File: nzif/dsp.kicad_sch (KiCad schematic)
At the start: 31 parts, among them U2 ADAU1467WBCPZ300

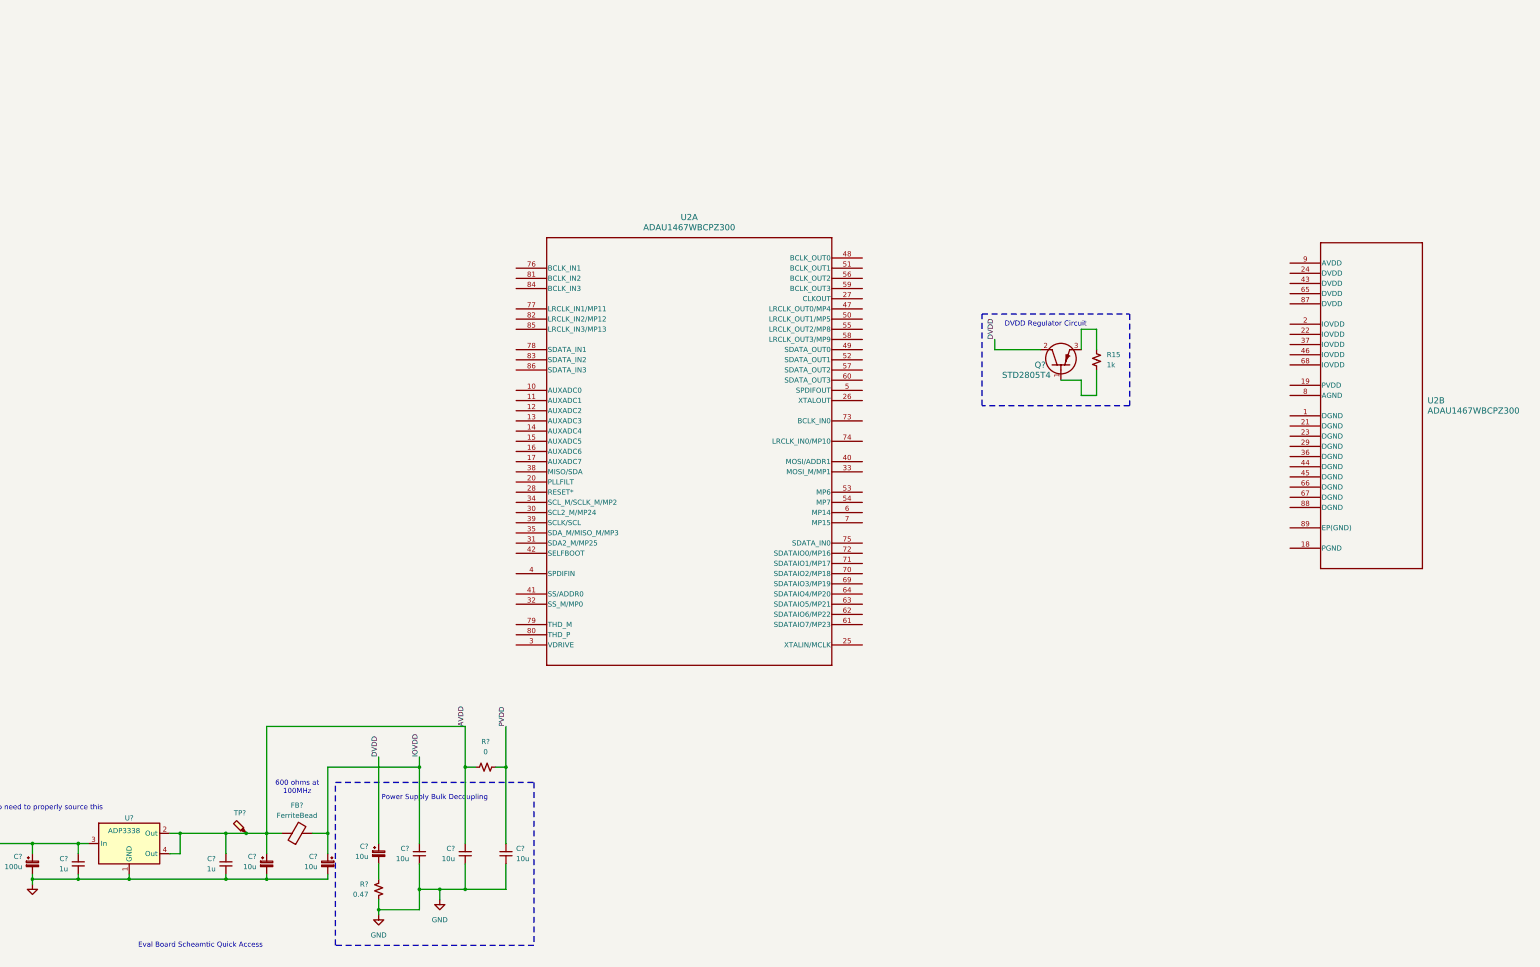
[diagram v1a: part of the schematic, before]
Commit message: Made adau1467 symbol klc compliant (ref #3)
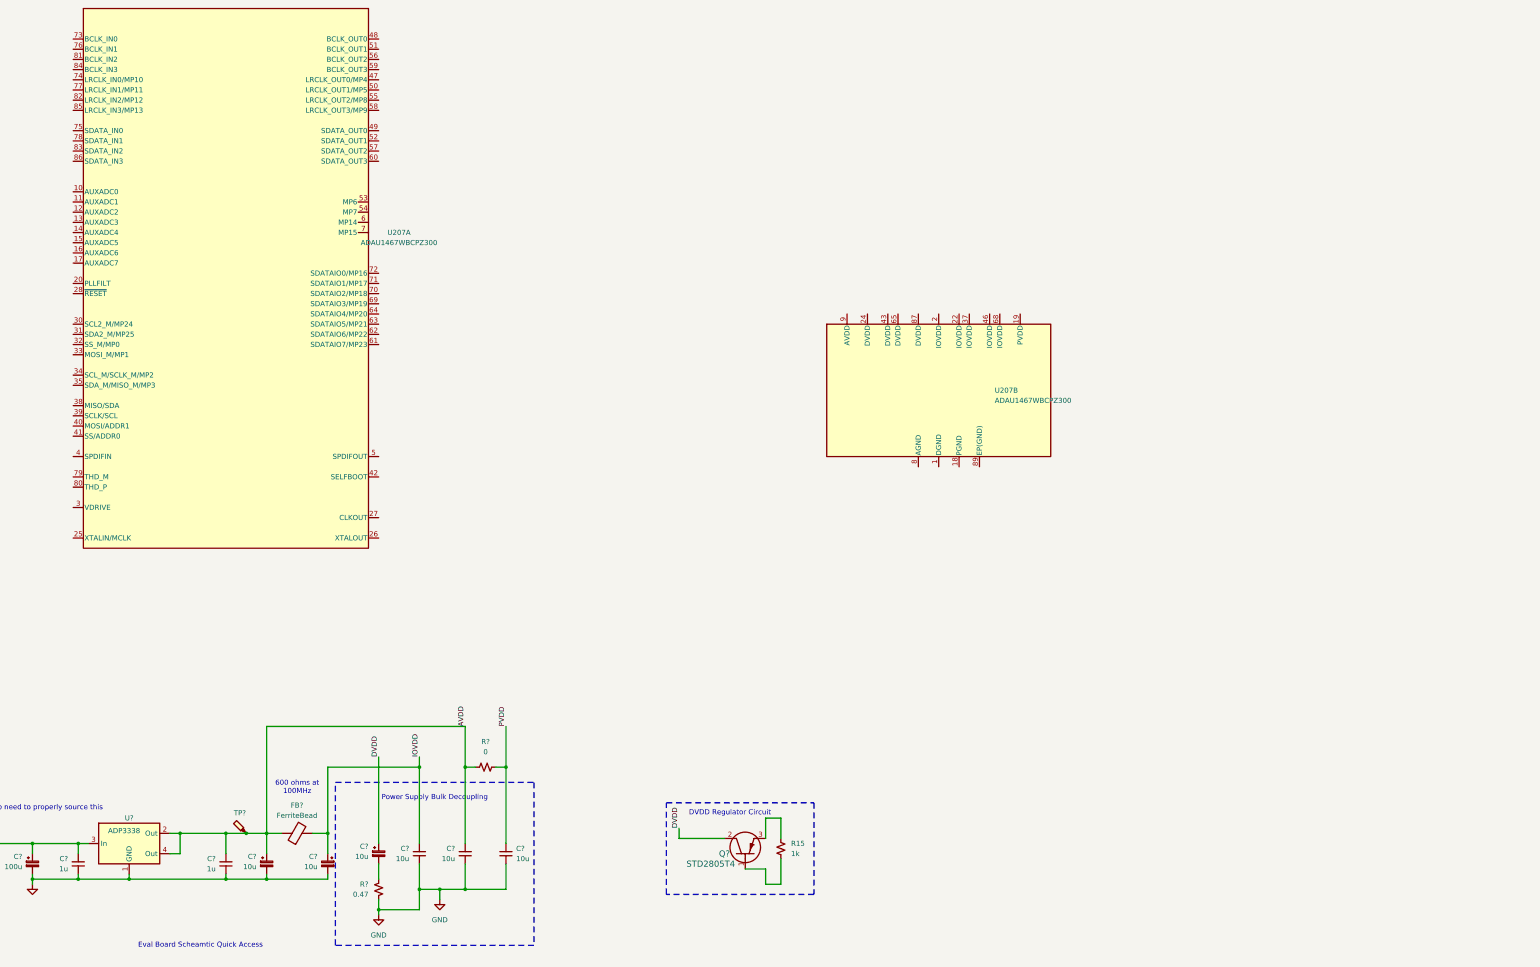
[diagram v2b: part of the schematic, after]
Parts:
- removed U2: ADAU1467WBCPZ300, CP_88_10_ADI, symbol ADAU1467:ADAU1467WBCPZ300
- added U207: ADAU1467WBCPZ300, CP_88_10_ADI, symbol nzif_radio_symbol_library:ADAU1467WBCPZ300
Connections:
- new net DGND: U207.1 (DGND), U207.21 (DGND), U207.23 (DGND), U207.29 (DGND), U207.36 (DGND), U207.44 (DGND), U207.45 (DGND), U207.66 (DGND), U207.67 (DGND), U207.88 (DGND)
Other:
- moved on the sheet: Q?, R15

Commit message: dsp tdm channels 0-2 added
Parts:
- removed R15: 1k, symbol Device:R_Small_US
- removed R?: 0, symbol Device:R_Small_US
- added C209, C211, C213, C215, C217, C219, C221, C223, C225, C227, C229: .1u, symbol Device:C_Small_US
- added C210, C212, C214, C216, C218, C220, C222, C224, C226, C228, C230: 10n, symbol Device:C_Small_US
- added J201: Conn_01x10, Connector_PinHeader_2.54mm:PinHeader_2x05_P2.54mm_Vertical, symbol Connector_Generic:Conn_01x10
- added R209: 1k, symbol Device:R_Small_US
- added R210, R211, R212, R213, R214, R215, R216, R217: 33, symbol Device:R_Small_US
- added TP201: VDrive, symbol Connector:TestPoint
- added TP202: IOVDD, symbol Connector:TestPoint
- added TP203: DVDD, symbol Connector:TestPoint
- Q?: footprint hf-transceiver:DPAKTO-252_TYPEA_STM -> nzif_footprints:DPAKTO-252_TYPEA_STM; symbol hf-transceiver:STD2805T4 -> nzif_radio_symbol_library:STD2805T4
- R?: value 0.47 -> 47
- U207: footprint CP_88_10_ADI -> nzif_footprints:CP_88_10_ADI
- U?: footprint hf-transceiver:RA_4_ADI -> nzif_footprints:RA_4_ADI; symbol hf-transceiver:ADM811TARTZ-REEL7 -> nzif-a:ADM811TARTZ-REEL7
- U?: symbol hf-transceiver:ADP3338 -> nzif_radio_symbol_library:ADP3338
- U?: footprint DFN-S8_6x5MC_MCH -> nzif_footprints:DPAKTO-252_TYPEA_STM; symbol hf-transceiver:25AA1024-I_MF -> nzif_radio_symbol_library:25AA1024-I_MF
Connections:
- net GND is gone; now on net DGND: C?.1, C?.1, C?.1, C?.1, C?.1, C?.1, C?.2, C?.2, C?.2, C?.2, D?.1 (K), J?.10 (Pin_10), R?.2, R?.2, SW?.2, U?.1 (GND), U?.1 (GND), U?.4 (VSS)
- net PVDD is gone; now on net 3.3V_DSP: C?.2
- net DGND: now also U207.18 (PGND), U207.8 (AGND), U207.89 (EP(GND)), C209.2, C210.2, C211.2, C212.2, C213.2, C214.2, C215.2, C216.2, C217.2, C218.2, C219.2, C220.2, C221.2, C222.2, C223.2, C224.2, C225.2, C226.2, C227.2, C228.2, C229.2, C230.2, J201.1 (Pin_1), J201.2 (Pin_2), J201.4 (Pin_4), J201.6 (Pin_6)
- net DVDD: now also U207.24 (DVDD), U207.43 (DVDD), U207.65 (DVDD), U207.87 (DVDD), C211.1, C212.1, C213.1, C214.1, C215.1, C216.1, C217.1, C218.1, TP203.1
- net IOVDD: now also Q?.3 (Emitter), U207.2 (IOVDD), U207.22 (IOVDD), U207.37 (IOVDD), U207.46 (IOVDD), U207.68 (IOVDD), C221.1, C222.1, C223.1, C224.1, C225.1, C226.1, C227.1, C228.1, C229.1, C230.1, R209.2, TP202.1; no longer C?.1, FB?.2
- net 3.3V_DSP: now reaches U207.19 (PVDD)
- net 3.3V_DSP: now also C?.2, U207.9 (AVDD), C209.1, C210.1, C219.1, C220.1
- net VDrive: now reaches Q?.1 (Base)
- net VDrive: now also R209.1, TP201.1
- net at U207.47 (LRCLK_OUT0/MP4): now also R210.2
- net at U207.48 (BCLK_OUT0): now also R211.2
- net at U207.50 (LRCLK_OUT1/MP5): now also R212.2
- net at U207.51 (BCLK_OUT1): now also R213.2
- net TDM1_SDIN_DAC: now reaches U207.52 (SDATA_OUT1)
- net at U207.55 (LRCLK_OUT2/MP8): now also R214.2
- net at U207.56 (BCLK_OUT2): now also R215.2
- net TDM2_SDIN_CODEC: now reaches U207.57 (SDATA_OUT2)
- net at U207.58 (LRCLK_OUT3/MP9): now also R216.2
- net at U207.59 (BCLK_OUT3): now also R217.2
- net TDM3_SDIN-HEAD: now reaches U207.60 (SDATA_OUT3)
- net TDM3_SDIN-HEAD: now also J201.8 (Pin_8)
- net TDM0_SDOUT_ADC: now reaches U207.75 (SDATA_IN0)
- net TDM2_SDOUT_CODEC: now reaches U207.83 (SDATA_IN2)
- net TDM3_SDOUT-HEAD: now reaches U207.86 (SDATA_IN3)
- net TDM3_SDOUT-HEAD: now also J201.7 (Pin_7)
- net AVDD: no longer names the net of C?.1, C?.2, FB?.1, TP?.1, U?.2 (Out), U?.4 (Out)
- net AVDD: no longer C?.2
- new net: C?.1, FB?.2
- new net BCLK_OUT0: R211.1
- new net BCLK_OUT1: R213.1
- new net BCLK_OUT2: R215.1
- new net BCLK_OUT3: J201.3 (Pin_3), R217.1
- new net LRCLK_OUT0: R210.1
- new net LRCLK_OUT1: R212.1
- new net LRCLK_OUT2: R214.1
- new net LRCLK_OUT3: J201.5 (Pin_5), R216.1
- no-connect marks 1 -> 13
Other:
- note added: "ADAU 1467 Eval Board"
- note added: "ADAU1467"
- note added: "Eval Board Fig 95 (pg 39 of pdf)- likely dont need"
- note added: "Power Supply Bulk Decoupling Eval Board pdf pg 33, Fig.81"
- note added: "TDM Port 0 ADC"
- note added: "TDM Port 1 DAC"
- note added: "TDM Port 2 CODEC"
- note added: "TDM Port 3 Header"
- note removed: "Eval Board Scheamtic Quick Access"
- note removed: "Power Supply Bulk Decoupling"
- moved on the sheet: C?, D?, FB?, J?, Q?, R?, SW?, TP?, U207A, U207B, U?

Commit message: updates to dsp (ref #3)
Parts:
- added J202: Conn_01x10, Connector_PinHeader_2.54mm:PinHeader_2x05_P2.54mm_Vertical, symbol Connector_Generic:Conn_01x10
- added R206: 33, symbol Device:R_Small_US
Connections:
- net BCLK_OUT3: now also J201.4 (Pin_4); no longer J201.3 (Pin_3)
- net DGND: now also J201.3 (Pin_3), J201.5 (Pin_5), J201.7 (Pin_7), J201.9 (Pin_9), U207.40 (MOSI/ADDR1), U207.41 (SS/ADDR0), J202.1 (Pin_1), J202.2 (Pin_2), J202.4 (Pin_4), J202.6 (Pin_6); no longer J201.2 (Pin_2), J201.4 (Pin_4), J201.6 (Pin_6)
- net LRCLK_OUT3: now also J201.6 (Pin_6); no longer J201.5 (Pin_5)
- net TDM3_SDIN-HEAD: now also J201.10 (Pin_10); no longer J201.8 (Pin_8)
- net TDM3_SDOUT-HEAD: now also J201.8 (Pin_8); no longer J201.7 (Pin_7)
- net at U207.27 (CLKOUT): now also R206.1
- net MISO_SDA: now reaches U207.38 (MISO/SDA)
- net SCLK/SCL: now reaches U207.39 (SCLK/SCL)
- new net MCLK: J201.2 (Pin_2), R206.2
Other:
- note added: "would a resistor array be suitable here?"
- moved on the sheet: J201

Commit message: Further connections to DSP (Ref #3 #25)
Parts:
- removed C? (x2): 10u, symbol Device:C_Polarized_Small
- removed C?: 100u, symbol Device:C_Polarized_Small
- removed C? (x2): 1u, symbol Device:C_Small
- removed D?: Green LED, symbol Device:LED_Small_Filled
- removed FB?: FerriteBead, symbol Device:FerriteBead
- removed J201, J202: Conn_01x10, Connector_PinHeader_2.54mm:PinHeader_2x05_P2.54mm_Vertical, symbol Connector_Generic:Conn_01x10
- removed J?: Conn_02x05_Odd_Even, symbol Connector_Generic:Conn_02x05_Odd_Even
- removed R? (x2): 10k, symbol Device:R_Small_US
- removed R?: ?, symbol Device:R_Small_US
- removed R?: 1k, symbol Device:R_Small_US
- removed TP?: TestPoint, symbol Connector:TestPoint_Probe
- removed U?: ADP3338, Package_TO_SOT_SMD:SOT-223, symbol nzif_radio_symbol_library:ADP3338
- added C231: 5.6n, symbol Device:C_Small_US
- added C232: 150p, symbol Device:C_Small_US
- added R207: 1k, symbol Device:R_Small_US
- added R220, R221, R222, R223, R224, R225: 33, symbol Device:R_Small_US
- added R226: 4.32k, symbol Device:R_Small_US
- added R227, R228: 10k, symbol Device:R_Small_US
- added TP204: THD_M, symbol Connector:TestPoint_Probe
- added TP205: THD_P, symbol Connector:TestPoint_Probe
- SW? (x2): footprint (none) -> Button_Switch_THT:SW_PUSH_6mm
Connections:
- net 3.3V_DSP: now also C231.1, C232.2
- net DGND: now also R228.2
- net IOVDD: now also R227.1
- net MCLK: now also U207.25 (XTALIN/MCLK); no longer R206.2
- net MOSI_M/MP1: now also U207.33 (MOSI_M/MP1)
- net MiSO_M: now also U207.35 (SDA_M/MISO_M/MP3)
- net SCLK_M: now also U207.34 (SCL_M/SCLK_M/MP2)
- net SELFBOOT: now also U207.42 (SELFBOOT), R228.1
- net SS_M/MP0: now also U207.32 (SS_M/MP0), R227.2
- net TDM0_SDOUT_ADC: now also R223.2; no longer U207.75 (SDATA_IN0)
- net TDM1_SDIN_DAC: now also R222.1; no longer U207.52 (SDATA_OUT1)
- net TDM2_SDIN_CODEC: now also R221.1; no longer U207.57 (SDATA_OUT2)
- net TDM2_SDOUT_CODEC: now also R224.2; no longer U207.83 (SDATA_IN2)
- net TDM3_SDIN-HEAD: now also R220.1; no longer U207.60 (SDATA_OUT3)
- net TDM3_SDOUT-HEAD: now also R225.2; no longer U207.86 (SDATA_IN3)
- net USB_~{RESET}: now also R207.2
- net VDrive: now also U207.3 (VDRIVE)
- net ~{RESET}: now also U207.28 (~{RESET})
- net at SW?.1, U?.3 (MR*): now also R207.1
- net DSP_AUX1_3v3: now reaches U207.10 (AUXADC0)
- net DSP_AUX1_GND: now reaches U207.11 (AUXADC1)
- net DSP_AUX1_AUX: now reaches U207.12 (AUXADC2)
- net DSP_AUX2_3v3: now reaches U207.13 (AUXADC3)
- net DSP_AUX2_GND: now reaches U207.14 (AUXADC4)
- net DSP_AUX2_AUX: now reaches U207.15 (AUXADC5)
- net DSP_AUX3_?: now reaches U207.16 (AUXADC6)
- net DSP_AUX3_??: now reaches U207.17 (AUXADC7)
- net PLL_FILT: now reaches U207.20 (PLLFILT)
- net PLL_FILT: now also C232.1, R226.2
- net DSP_MP24: now reaches U207.30 (SCL2_M/MP24)
- net DSP_MP24: now also U207.61 (SDATAIO7/MP23), U207.62 (SDATAIO6/MP22), U207.63 (SDATAIO5/MP21), U207.64 (SDATAIO4/MP20), U207.69 (SDATAIO3/MP19), U207.70 (SDATAIO2/MP18), U207.71 (SDATAIO1/MP17), U207.72 (SDATAIO0/MP16)
- net DSP_MP25: now reaches U207.31 (SDA2_M/MP25)
- net DSP_MP06: now reaches U207.53 (MP6)
- net DSP_MP07: now reaches U207.54 (MP7)
- net DSP_MP14: now reaches U207.6 (MP14)
- net DSP_MP15: now reaches U207.7 (MP15)
- net at U207.79 (THD_M): now also TP204.1
- net at U207.80 (THD_P): now also TP205.1
- new net: R225.1, U207.86 (SDATA_IN3)
- new net: R220.2, U207.60 (SDATA_OUT3)
- new net: R224.1, U207.83 (SDATA_IN2)
- new net: C231.2, R226.1
- new net: R221.2, U207.57 (SDATA_OUT2)
- new net: R222.2, U207.52 (SDATA_OUT1)
- new net: R223.1, U207.75 (SDATA_IN0)
- new net DSP_MCLK: R206.2
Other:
- note added: "All MP/GIPO go to header on top sheet"
- note added: "Aux pins to header on top sheet"
- note added: "Eval board used FSM6JSMA for the switch. SMD. maybe switch to that. Also do we need USB_RESET (diode)> Did not include SDP Reset"
- note added: "PLL Loop Filter"
- note added: "Self Boot Circuit / EEPROM This guy is SPI, so check connections to 1467 Should we add an LED?"
- note added: "TDM port 3 goes to header on top sheet"
- note removed: "600 ohms at 100MHz"
- note removed: "Eval Board Fig 95 (pg 39 of pdf)- likely dont need"
- note removed: "Going to need to properly source this"
- note removed: "SPI 10 Pin Connector"
- note removed: "Self Boot Circuit"
- moved on the sheet: SW?

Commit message: fix dsp to be on 100mil grid (Ref #3 #25)
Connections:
- net SS_M/MP0 is gone; now on net MiSO_M: R227.2, U207.32 (SS_M/MP0), U?.1 (*CS)
- net MiSO_M: now also R?.2, U?.3 (*WP)
- net at R217.2: now also U207.58 (LRCLK_OUT3/MP9); no longer U207.59 (BCLK_OUT3)
- net at R216.2: now also U207.59 (BCLK_OUT3); no longer U207.58 (LRCLK_OUT3/MP9)
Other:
- note added: "Who gets xtal out"
- moved on the sheet: C219, C220, C232, C?, Q?, R206, R209, R210, R211, R212, R213, R214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
